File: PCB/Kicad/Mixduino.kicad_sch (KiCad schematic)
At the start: 5 parts

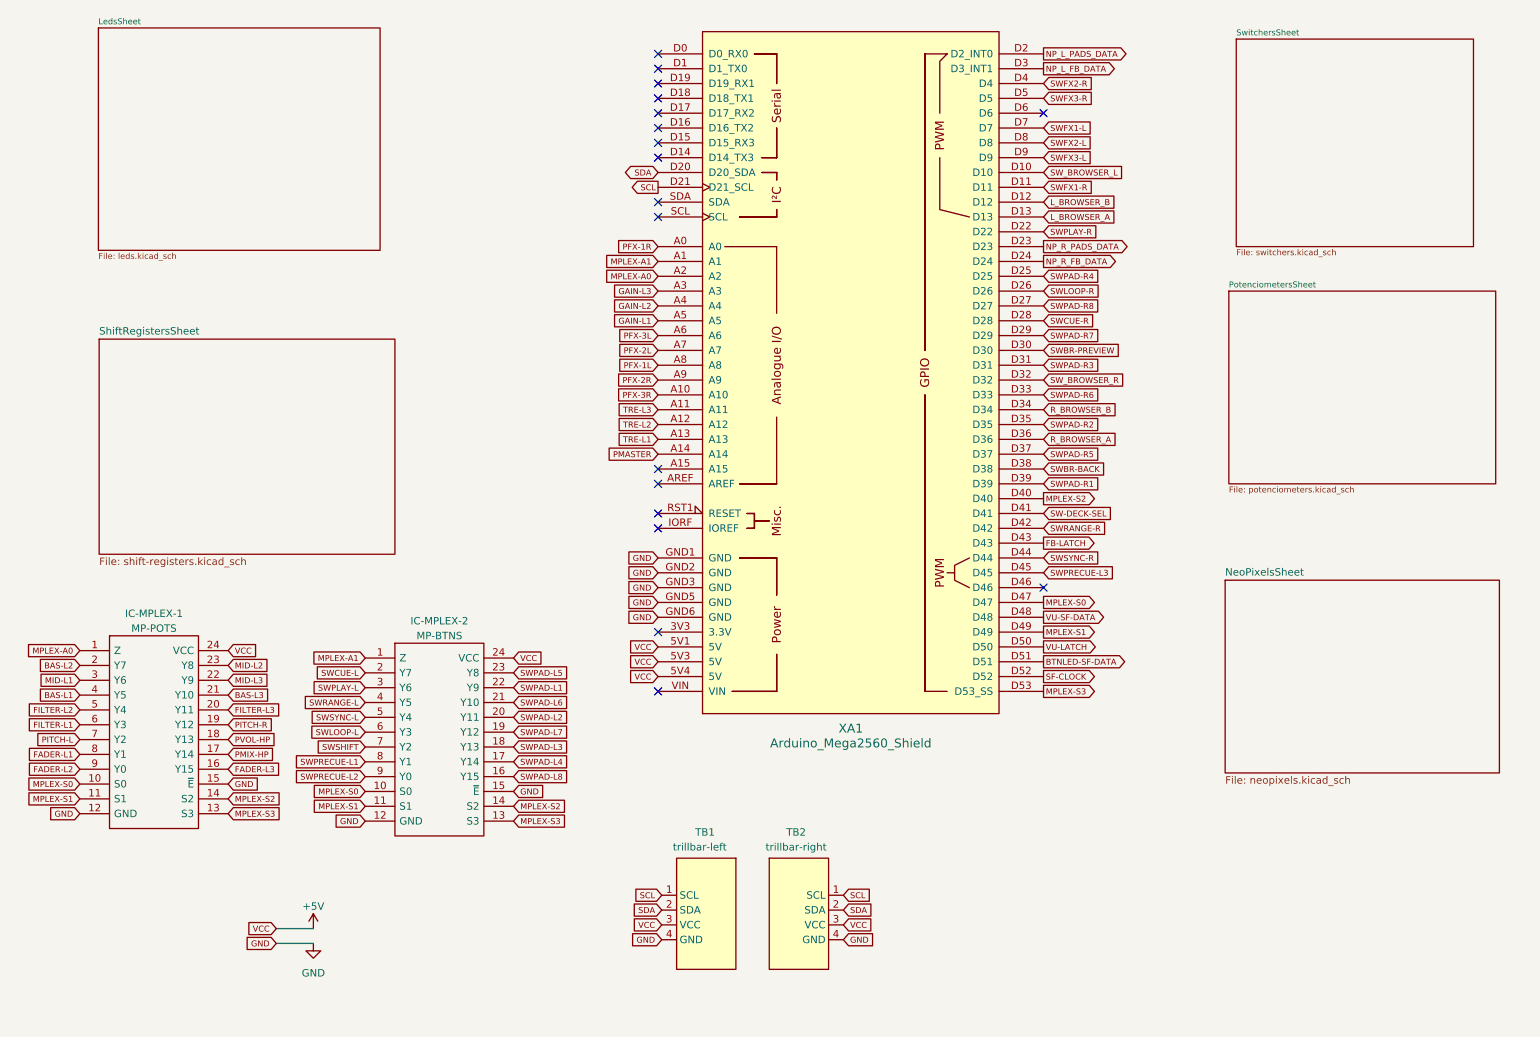
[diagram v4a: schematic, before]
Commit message: all neopixels together
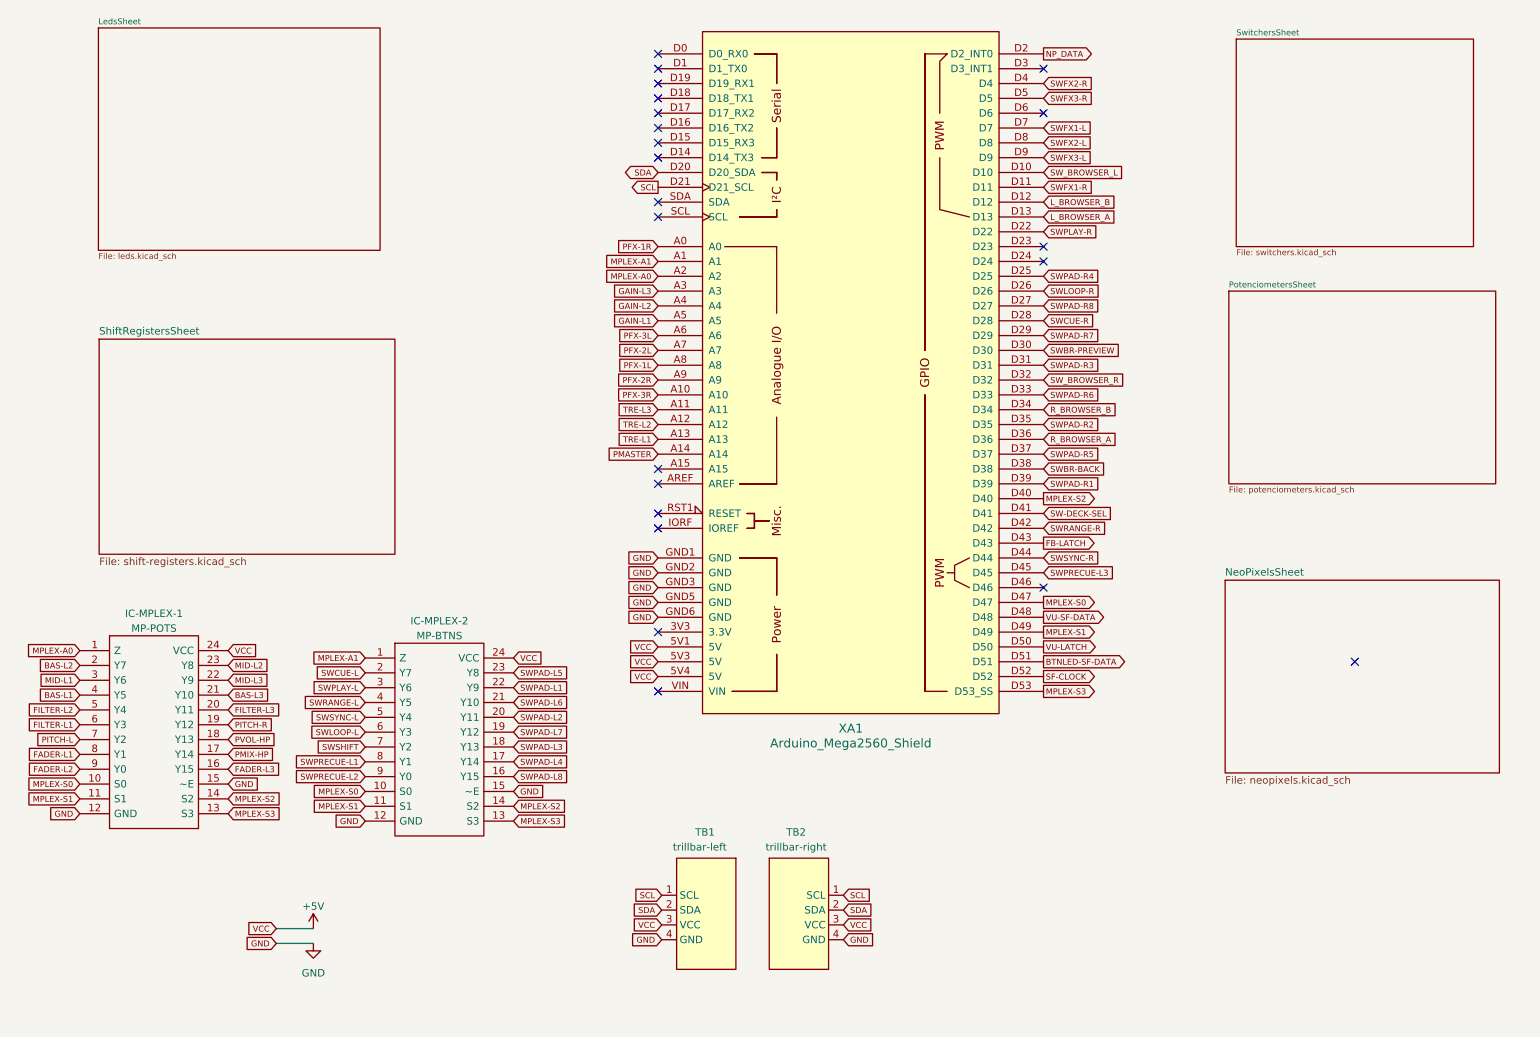
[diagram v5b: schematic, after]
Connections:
- net NP_L_FB_DATA: no longer names the net of XA1.D3 (D3_INT1)
- net NP_L_PADS_DATA renamed NP_DATA
- net NP_R_FB_DATA: no longer names the net of XA1.D24
- net NP_R_PADS_DATA: no longer names the net of XA1.D23
- no-connect marks 18 -> 22
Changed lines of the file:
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@@
-(kicad_sch (version 20210406) (generator eeschema)
+(kicad_sch (version 20210615) (generator eeschema)
   (paper "A4")
   (no_connect (at 127.635 28.575))
@@
   (no_connect (at 127.635 127.635))
   (no_connect (at 127.635 137.795))
+  (no_connect (at 193.675 31.115))
   (no_connect (at 193.675 38.735))
+  (no_connect (at 193.675 61.595))
+  (no_connect (at 193.675 64.135))
   (no_connect (at 193.675 120.015))
+  (no_connect (at 247.015 132.715))
   (wire (pts (xy 62.23 178.435) (xy 68.58 178.435))
     (stroke (width 0) (type solid) (color 0 0 0 0))
@@
     )
   )
-  (global_label "NP_L_PADS_DATA" (shape output) (at 193.675 28.575 0)
+  (global_label "NP_DATA" (shape output) (at 193.675 28.575 0)
     (effects (font (size 1.016 1.016)) (justify left))
     (property "Intersheet References" "${INTERSHEET_REFS}" (id 0) (at 180.4718 28.5115 0)
-      (effects (font (size 1.016 1.016)) (justify right) hide)
-    )
-  )
-  (global_label "NP_L_FB_DATA" (shape output) (at 193.675 31.115 0)
-    (effects (font (size 1.016 1.016)) (justify left))
-    (property "Intersheet References" "${INTERSHEET_REFS}" (id 0) (at 180.4718 31.0515 0)
       (effects (font (size 1.016 1.016)) (justify right) hide)
     )
@@
     (property "Intersheet References" "${INTERSHEET_REFS}" (id 0) (at 47.625 26.035 0)
       (effects (font (size 1.27 1.27)) hide)
-    )
-  )
-  (global_label "NP_R_PADS_DATA" (shape output) (at 193.675 61.595 0)
-    (effects (font (size 1.016 1.016)) (justify left))
-    (property "Intersheet References" "${INTERSHEET_REFS}" (id 0) (at 180.2783 61.5315 0)
-      (effects (font (size 1.016 1.016)) (justify right) hide)
-    )
-  )
-  (global_label "NP_R_FB_DATA" (shape output) (at 193.675 64.135 0)
-    (effects (font (size 1.016 1.016)) (justify left))
-    (property "Intersheet References" "${INTERSHEET_REFS}" (id 0) (at 180.2783 64.0715 0)
-      (effects (font (size 1.016 1.016)) (justify right) hide)
     )
   )
@@
       (reference "NPR1") (unit 1) (value "L-NP-PADS_R") (footprint "Library:R_1206_3216Metric_Pad1.30x1.75mm_HandSolder")
     )
-    (path "/27ec6e33-6a27-4865-8f8e-aab38be2398e/6107c0ab-f01d-4f9c-8778-fb853a8da67f"
-      (reference "NPR2") (unit 1) (value "R-NP-PADS_R") (footprint "Library:R_1206_3216Metric_Pad1.30x1.75mm_HandSolder")
-    )
-    (path "/27ec6e33-6a27-4865-8f8e-aab38be2398e/36dfd4e4-2187-424f-a46a-2e3c312070f0"
-      (reference "NPR3") (unit 1) (value "L-NP-FB_R") (footprint "Library:R_1206_3216Metric_Pad1.30x1.75mm_HandSolder")
-    )
-    (path "/27ec6e33-6a27-4865-8f8e-aab38be2398e/2e9bf44d-59d5-47da-9cae-7ece8504d321"
-      (reference "NPR4") (unit 1) (value "R-NP-FB_R") (footprint "Library:R_1206_3216Metric_Pad1.30x1.75mm_HandSolder")
-    )
     (path "/00000000-0000-0000-0000-000060683d75/00000000-0000-0000-0000-0000606dfaaa"

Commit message: changed encoders pins to interrupt pins
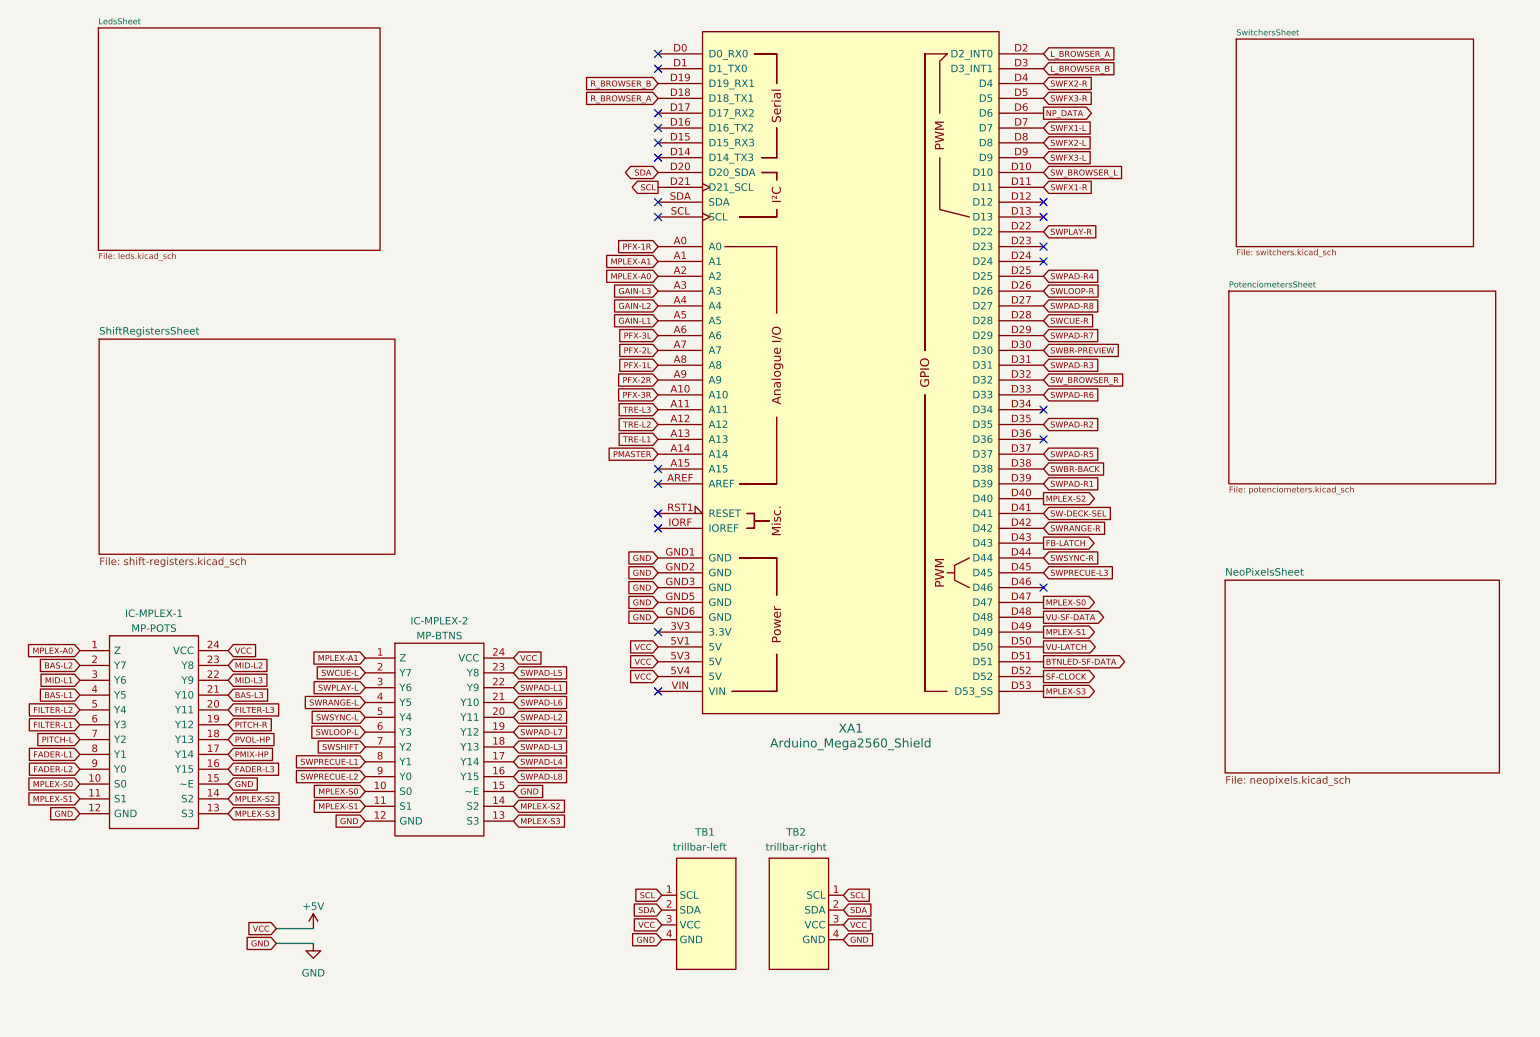
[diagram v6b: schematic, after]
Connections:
- net L_BROWSER_A: now also XA1.D2 (D2_INT0); no longer XA1.D13
- net L_BROWSER_B: now also XA1.D3 (D3_INT1); no longer XA1.D12
- net NP_DATA: now also XA1.D6; no longer XA1.D2 (D2_INT0)
- net R_BROWSER_A: now also XA1.D18 (D18_TX1); no longer XA1.D36
- net R_BROWSER_B: now also XA1.D19 (D19_RX1); no longer XA1.D34
- no-connect marks 22 -> 21
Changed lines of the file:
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@@
   (no_connect (at 127.635 28.575))
   (no_connect (at 127.635 31.115))
-  (no_connect (at 127.635 33.655))
-  (no_connect (at 127.635 36.195))
   (no_connect (at 127.635 38.735))
   (no_connect (at 127.635 41.275))
@@
   (no_connect (at 127.635 127.635))
   (no_connect (at 127.635 137.795))
-  (no_connect (at 193.675 31.115))
-  (no_connect (at 193.675 38.735))
+  (no_connect (at 193.675 53.975))
+  (no_connect (at 193.675 56.515))
   (no_connect (at 193.675 61.595))
   (no_connect (at 193.675 64.135))
+  (no_connect (at 193.675 89.535))
+  (no_connect (at 193.675 94.615))
   (no_connect (at 193.675 120.015))
-  (no_connect (at 247.015 132.715))
   (wire (pts (xy 62.23 178.435) (xy 68.58 178.435))
     (stroke (width 0) (type solid) (color 0 0 0 0))
@@
     )
   )
+  (global_label "R_BROWSER_B" (shape input) (at 127.635 33.655 180)
+    (effects (font (size 1.016 1.016)) (justify right))
+    (property "Intersheet References" "${INTERSHEET_REFS}" (id 0) (at 116.7541 33.7185 0)
+      (effects (font (size 1.016 1.016)) (justify right) hide)
+    )
+  )
+  (global_label "R_BROWSER_A" (shape input) (at 127.635 36.195 180)
+    (effects (font (size 1.016 1.016)) (justify right))
+    (property "Intersheet References" "${INTERSHEET_REFS}" (id 0) (at 116.8993 36.2585 0)
+      (effects (font (size 1.016 1.016)) (justify right) hide)
+    )
+  )
   (global_label "SDA" (shape bidirectional) (at 127.635 48.895 180)
     (effects (font (size 1.016 1.016)) (justify right))
@@
     )
   )
-  (global_label "NP_DATA" (shape output) (at 193.675 28.575 0)
-    (effects (font (size 1.016 1.016)) (justify left))
-    (property "Intersheet References" "${INTERSHEET_REFS}" (id 0) (at 180.4718 28.5115 0)
-      (effects (font (size 1.016 1.016)) (justify right) hide)
+  (global_label "L_BROWSER_A" (shape input) (at 193.675 28.575 0)
+    (effects (font (size 1.016 1.016)) (justify left))
+    (property "Intersheet References" "${INTERSHEET_REFS}" (id 0) (at 204.4107 28.5115 0)
+      (effects (font (size 1.016 1.016)) (justify left) hide)
+    )
+  )
+  (global_label "L_BROWSER_B" (shape input) (at 193.675 31.115 0)
+    (effects (font (size 1.016 1.016)) (justify left))
+    (property "Intersheet References" "${INTERSHEET_REFS}" (id 0) (at 204.5559 31.0515 0)
+      (effects (font (size 1.016 1.016)) (justify left) hide)
     )
   )
@@
     )
   )
+  (global_label "NP_DATA" (shape output) (at 193.675 38.735 0)
+    (effects (font (size 1.016 1.016)) (justify left))
+    (property "Intersheet References" "${INTERSHEET_REFS}" (id 0) (at 180.4718 38.6715 0)
+      (effects (font (size 1.016 1.016)) (justify right) hide)
+    )
+  )
   (global_label "SWFX1-L" (shape input) (at 193.675 41.275 0)
     (effects (font (size 1.016 1.016)) (justify left))
@@
     (property "Intersheet References" "${INTERSHEET_REFS}" (id 0) (at 47.625 -62.865 0)
       (effects (font (size 1.27 1.27)) (justify right) hide)
-    )
-  )
-  (global_label "L_BROWSER_B" (shape input) (at 193.675 53.975 0)
-    (effects (font (size 1.016 1.016)) (justify left))
-    (property "Intersheet References" "${INTERSHEET_REFS}" (id 0) (at 204.5559 53.9115 0)
-      (effects (font (size 1.016 1.016)) (justify left) hide)
-    )
-  )
-  (global_label "L_BROWSER_A" (shape input) (at 193.675 56.515 0)
-    (effects (font (size 1.016 1.016)) (justify left))
-    (property "Intersheet References" "${INTERSHEET_REFS}" (id 0) (at 204.4107 56.4515 0)
-      (effects (font (size 1.016 1.016)) (justify left) hide)
     )
   )
@@
     )
   )
-  (global_label "R_BROWSER_B" (shape input) (at 193.675 89.535 0)
-    (effects (font (size 1.016 1.016)) (justify left))
-    (property "Intersheet References" "${INTERSHEET_REFS}" (id 0) (at 204.5559 89.4715 0)
-      (effects (font (size 1.016 1.016)) (justify left) hide)
-    )
-  )
   (global_label "SWPAD-R2" (shape input) (at 193.675 92.075 0)
     (effects (font (size 1.016 1.016)) (justify left))
     (property "Intersheet References" "${INTERSHEET_REFS}" (id 0) (at 117.475 141.605 0)
       (effects (font (size 1.27 1.27)) (justify right) hide)
-    )
-  )
-  (global_label "R_BROWSER_A" (shape input) (at 193.675 94.615 0)
-    (effects (font (size 1.016 1.016)) (justify left))
-    (property "Intersheet References" "${INTERSHEET_REFS}" (id 0) (at 204.4107 94.5515 0)
-      (effects (font (size 1.016 1.016)) (justify left) hide)
     )
   )
@@
   (sheet (at 31.75 24.13) (size 48.26 38.1)
     (stroke (width 0) (type solid) (color 0 0 0 0))
-    (fill (color 72 72 72 0.0000))
+    (fill (color 0 0 0 0.0000))
     (property "Sheet name" "LedsSheet" (id 0) (at 31.75 23.6215 0)
       (effects (font (size 1.016 1.016)) (justify left bottom))
@@
   (sheet (at 31.877 77.4446) (size 50.673 36.8554)
     (stroke (width 0) (type solid) (color 0 0 0 0))
-    (fill (color 72 72 72 0.0000))
+    (fill (color 0 0 0 0.0000))
     (property "Sheet name" "ShiftRegistersSheet" (id 0) (at 31.877 76.8091 0)
       (effects (font (size 1.27 1.27)) (justify left bottom))
@@
   (sheet (at 226.695 26.035) (size 40.64 35.56)
     (stroke (width 0) (type solid) (color 0 0 0 0))
-    (fill (color 72 72 72 0.0000))
+    (fill (color 0 0 0 0.0000))
     (property "Sheet name" "SwitchersSheet" (id 0) (at 226.695 25.5265 0)
       (effects (font (size 1.016 1.016)) (justify left bottom))

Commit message: adding ics WIP
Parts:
- removed IC-MPLEX-1: MP-POTS, Library:SOIC-24W_7.5x15.4mm_P1.27mm, symbol mixduino-mk2:74HC4067D,653
- removed IC-MPLEX-2: MP-BTNS, Library:SOIC-24W_7.5x15.4mm_P1.27mm, symbol mixduino-mk2:74HC4067D,653
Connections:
- net GAIN-L1: no longer names the net of XA1.A5
- net GAIN-L2: no longer names the net of XA1.A4
- net GAIN-L3: no longer names the net of XA1.A3
- net PFX-1L: no longer names the net of XA1.A8
- net PFX-2L: no longer names the net of XA1.A7
- net PFX-2R: no longer names the net of XA1.A9
- net PFX-3L: no longer names the net of XA1.A6
- net PFX-3R: no longer names the net of XA1.A10
- net SW-DECK-SEL: no longer names the net of XA1.D41
- net SWCUE-R: no longer names the net of XA1.D28
- net SWLOOP-R: no longer names the net of XA1.D26
- net SWPAD-R1: no longer names the net of XA1.D39
- net SWPAD-R2: no longer names the net of XA1.D35
- net SWPAD-R3: no longer names the net of XA1.D31
- net SWPAD-R4: no longer names the net of XA1.D25
- net SWPAD-R5: no longer names the net of XA1.D37
- net SWPAD-R6: no longer names the net of XA1.D33
- net SWPAD-R7: no longer names the net of XA1.D29
- net SWPAD-R8: no longer names the net of XA1.D27
- net SWPLAY-R: no longer names the net of XA1.D22
- net SWPRECUE-L3: no longer names the net of XA1.D45
- net SWRANGE-R: no longer names the net of XA1.D42
- net SWSYNC-R: no longer names the net of XA1.D44
- net TRE-L1: no longer names the net of XA1.A13
- net TRE-L2: no longer names the net of XA1.A12
- net TRE-L3: no longer names the net of XA1.A11
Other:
- added sheet MultiplexersSheet (multiplexers.kicad_sch)
